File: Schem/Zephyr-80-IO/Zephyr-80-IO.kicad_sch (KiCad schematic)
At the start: 0 parts

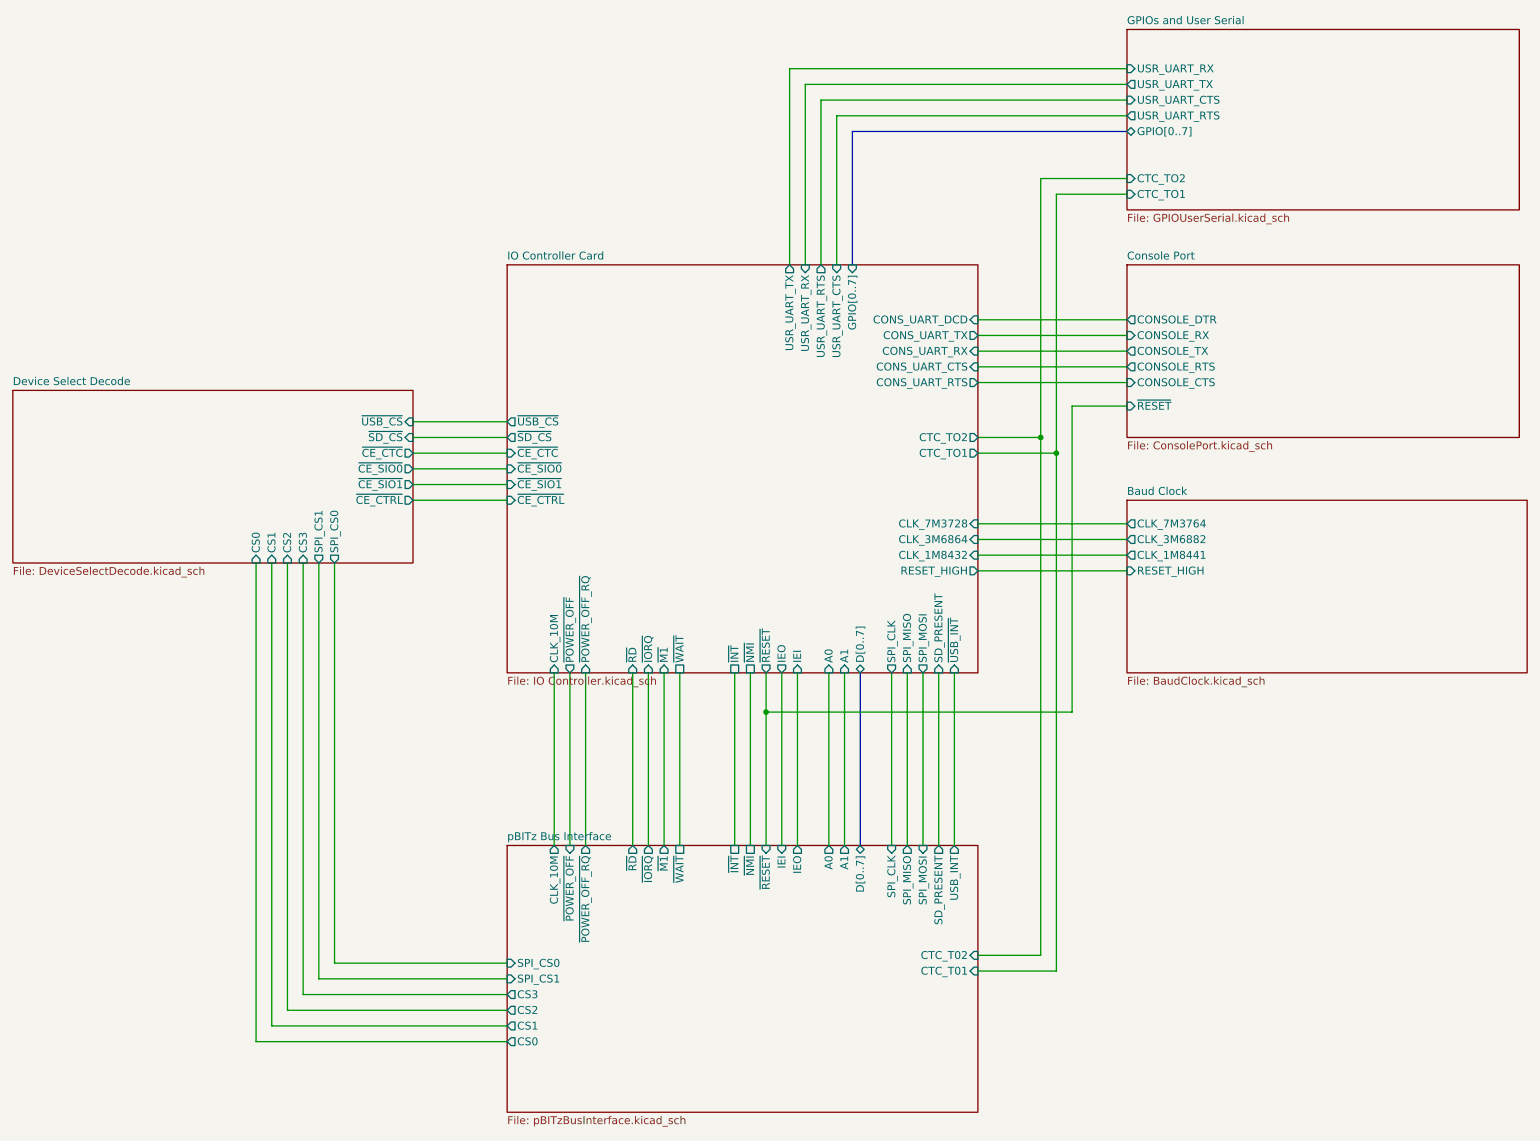
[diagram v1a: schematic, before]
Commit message: Updated the IO Controller to properly support SDLC and SPI.
* Separated SPI1 and SPI2 and associated to the right pins.
      SPI1 is for devices (USB, SD Card and Controllers)
      SPI2 is for the SDLC controller (Z80 SIO1/A and B)

* Fixed the 1.27mm vs 2.54mm pin headers
* Fixed the power sequencing
* Fixed the pull ups
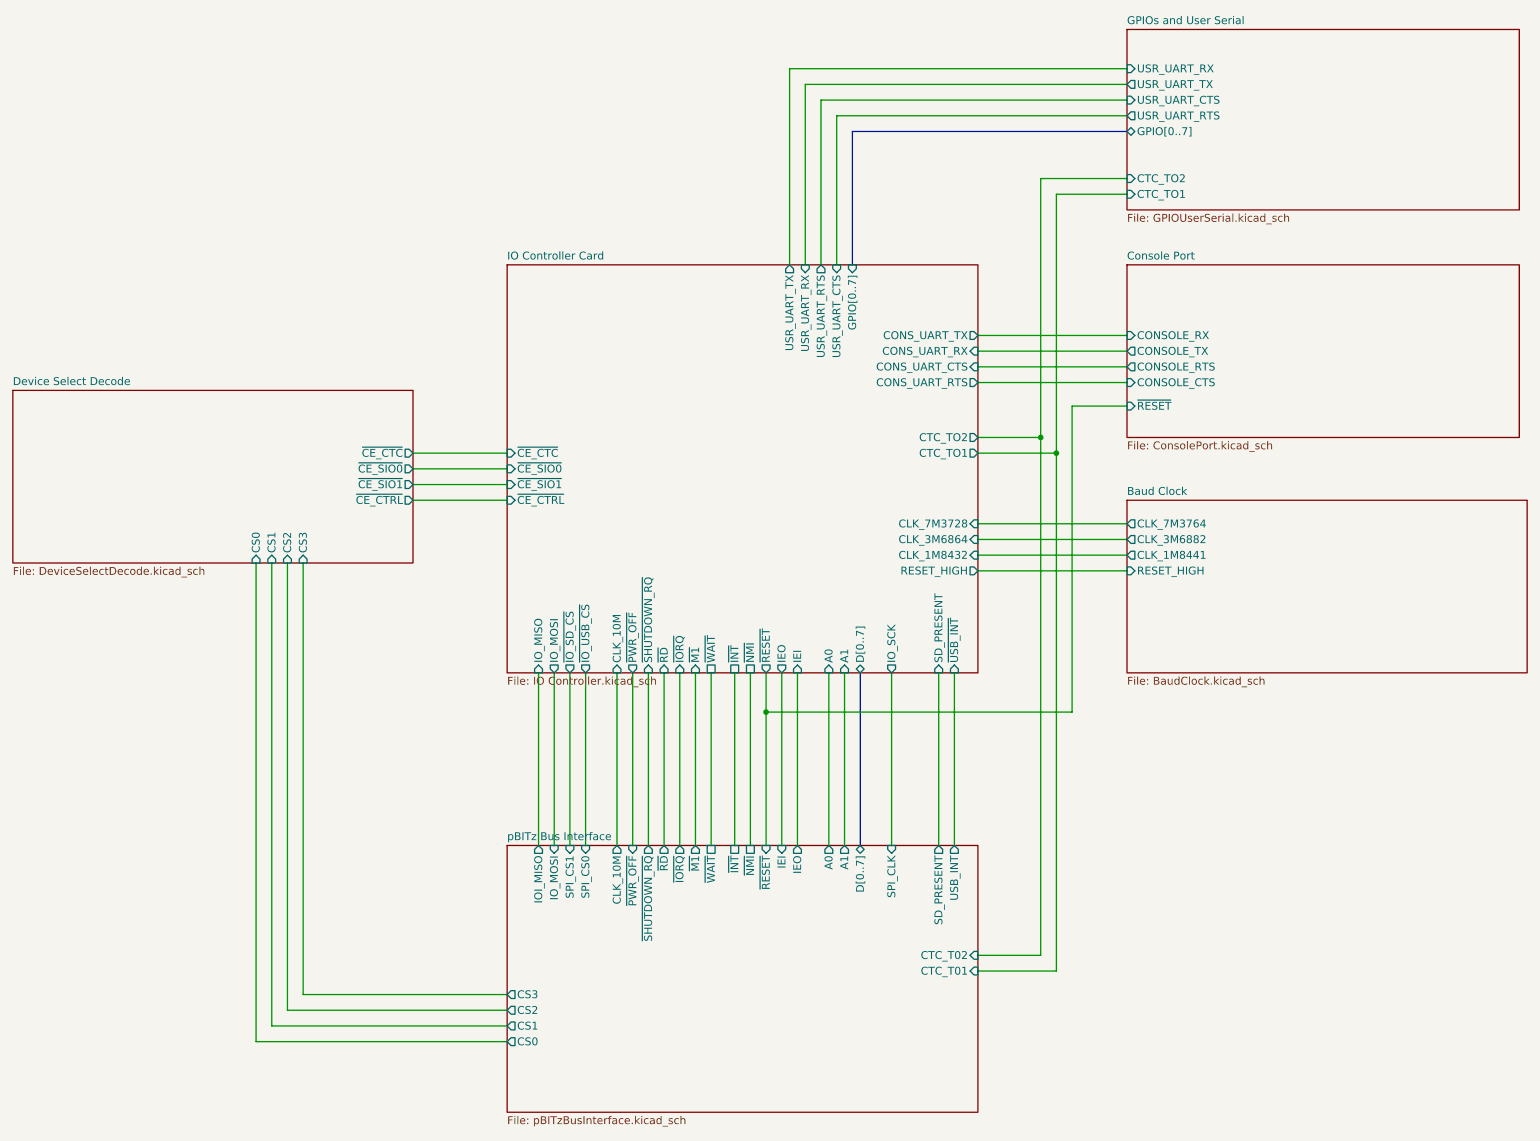
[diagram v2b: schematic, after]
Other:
- sheet Console Port ports: added none; removed CONSOLE_DTR
- sheet Device Select Decode ports: added none; removed SPI_CS0, SPI_CS1, ~{SD_CS}, ~{USB_CS}
- sheet IO Controller Card ports: added IO_MISO, IO_MOSI, IO_SCK, ~{IO_SD_CS}, ~{IO_USB_CS}, ~{PWR_OFF}, ~{SHUTDOWN_RQ}; removed CONS_UART_DCD, SPI_CLK, SPI_MISO, SPI_MOSI, ~{POWER_OFF_RQ}, ~{POWER_OFF}, ~{SD_CS}, ~{USB_CS}
- sheet pBITz Bus Interface ports: added IOI_MISO, IO_MOSI, ~{PWR_OFF}, ~{SHUTDOWN_RQ}; removed SPI_MISO, SPI_MOSI, ~{POWER_OFF_RQ}, ~{POWER_OFF}

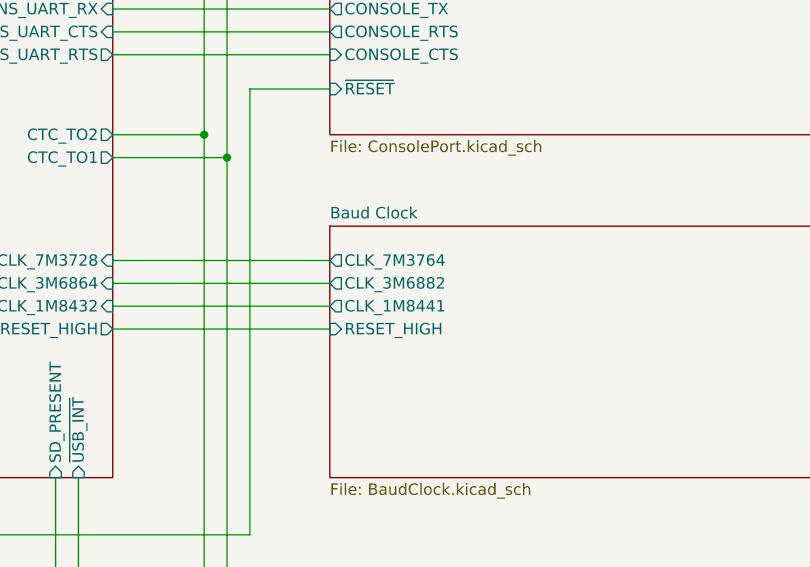
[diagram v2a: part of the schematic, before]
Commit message: Fixed a few mistakes in the IO Controller
* Wrong layer for vertical traces (should not be on the same layer as vcc plane)
* Added pull-downs for DCD for all SIOs (we don't use this line)
* Connected DCD and CTS to the MCU for SIO1 in case we want to use it to gate the SIO1
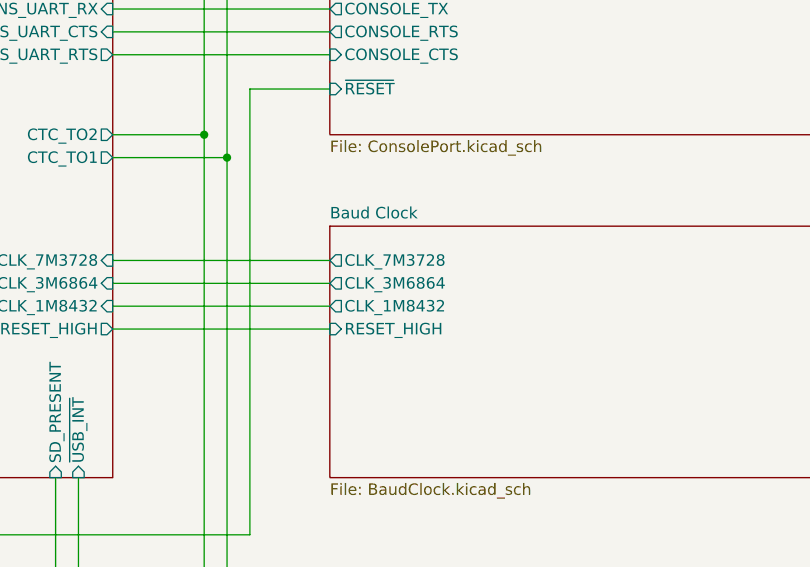
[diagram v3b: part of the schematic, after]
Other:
- sheet Baud Clock ports: added CLK_1M8432, CLK_3M6864, CLK_7M3728; removed CLK_1M8441, CLK_3M6882, CLK_7M3764
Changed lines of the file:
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@@
-			)
-		)
-		(pin "CLK_3M6882" output
-			(at 392.43 175.26 180)
-			(effects
-				(font
-					(size 1.27 1.27)
-				)
-				(justify left)
-			)
-		)
-		(pin "CLK_1M8441" output
-			(at 392.43 177.8 180)
-			(effects
-				(font
-					(size 1.27 1.27)
-				)
-				(justify left)
 			)
 		)
@@
 			)
 		)
-		(pin "CLK_7M3764" output
+		(pin "CLK_7M3728" output
 			(at 392.43 172.72 180)
 			(effects
 				(font
+					(size 1.27 1.27)
+				)
+				(justify left)
+			)
+		)
+		(pin "CLK_3M6864" output
+			(at 392.43 175.26 180)
+			(effects
+				(font
+					(size 1.27 1.27)
+				)
+				(justify left)
+			)
+		)
+		(pin "CLK_1M8432" output
+			(at 392.43 177.8 180)
+			(effects
+				(font
